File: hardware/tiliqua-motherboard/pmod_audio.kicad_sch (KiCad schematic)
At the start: 1 part, among them J1 Conn_01x15

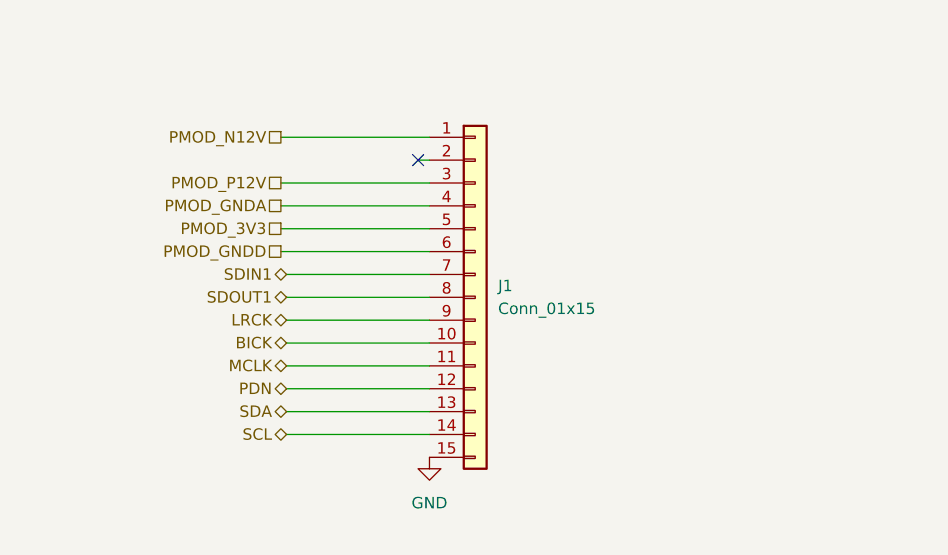
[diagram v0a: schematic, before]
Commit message: hardware/r2: squash in all changes for tiliqua R2 (#17)
* squash in all changes for Tiliqua R2
* add schematics for all components of Tiliqua R2
* update README and add lightbox photos
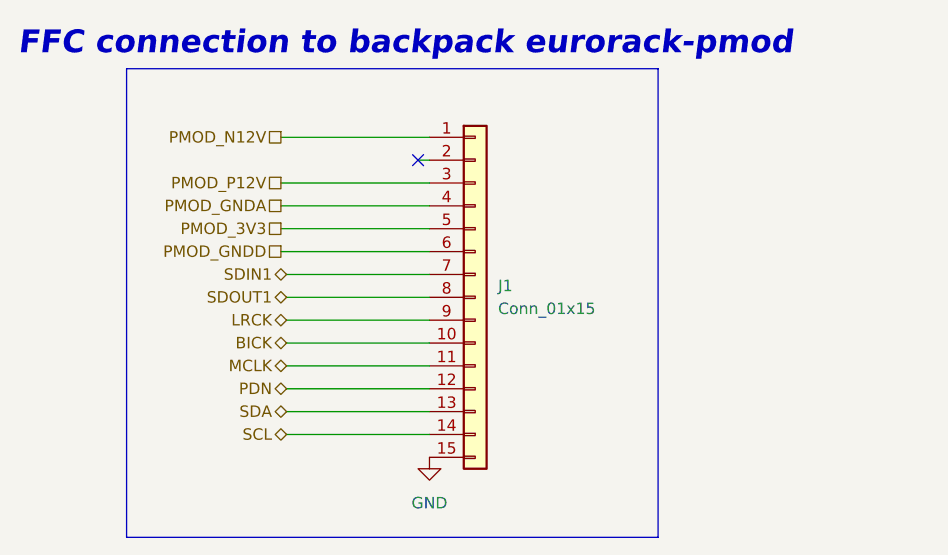
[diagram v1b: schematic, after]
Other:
- note added: "FFC connection to backpack eurorack-pmod"
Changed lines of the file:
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@@
+		)
+	)
+	(rectangle
+		(start 99.695 48.26)
+		(end 158.75 100.33)
+		(stroke
+			(width 0)
+			(type default)
+		)
+		(fill
+			(type none)
+		)
+	)
+	(text "FFC connection to backpack eurorack-pmod"
+		(exclude_from_sim no)
+		(at 87.63 46.99 0)
+		(effects
+			(font
+				(size 2.54 2.54)
+				(thickness 0.508)
+				(bold yes)
+				(italic yes)
+			)
+			(justify left bottom)
 		)
 	)
@@
 		)
 		(instances
-			(project "backpack"
+			(project "tiliqua-motherboard"
 				(path "/df6062c3-a570-4505-924c-c7fe32df3670/830acc84-6e16-4cb8-9214-1acea5145425"
 					(reference "#PWR067")
@@
 			)
 		)
+		(property "Tol" ""
+			(at 138.43 73.66 0)
+			(effects
+				(font
+					(size 1.27 1.27)
+				)
+				(hide yes)
+			)
+		)
 		(pin "5"
 		)
@@
 		)
 		(instances
-			(project "backpack"
+			(project "tiliqua-motherboard"
 				(path "/df6062c3-a570-4505-924c-c7fe32df3670/830acc84-6e16-4cb8-9214-1acea5145425"
 					(reference "J1")
